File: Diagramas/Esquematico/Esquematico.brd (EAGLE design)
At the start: 64 x 80 mm, 48 parts, among them IC3 DS3231N_DIP, IC4 3071_SMD, J1 Modulo Pir, J2 RASPBERRYPI-40-PIN-GPIO_SMT, K1 SRD-05VDC-SL-C, K2 SRD-05VDC-SL-C, K3 SRD-05VDC-SL-C, K4 SRD-05VDC-SL-C, U1 RFM69HW-868S2

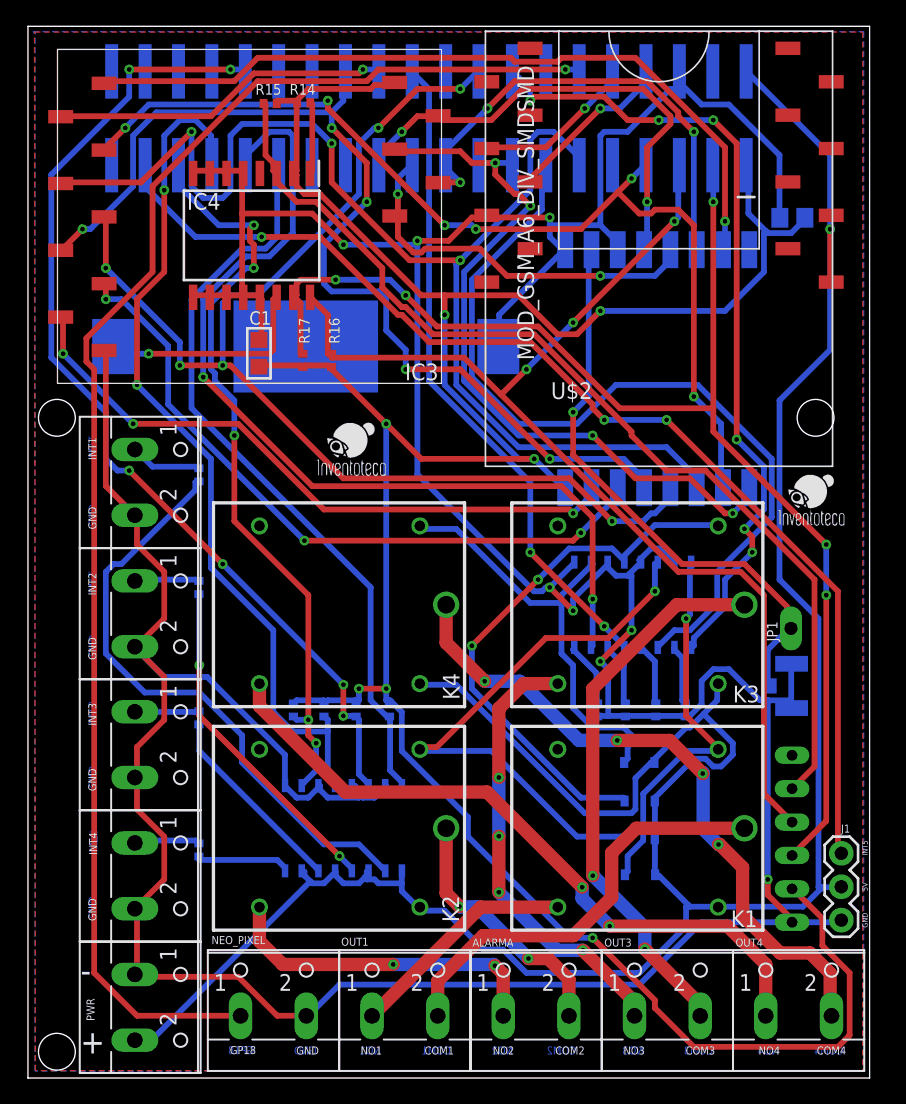
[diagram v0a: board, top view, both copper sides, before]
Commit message: Modulo Lora Eliminado
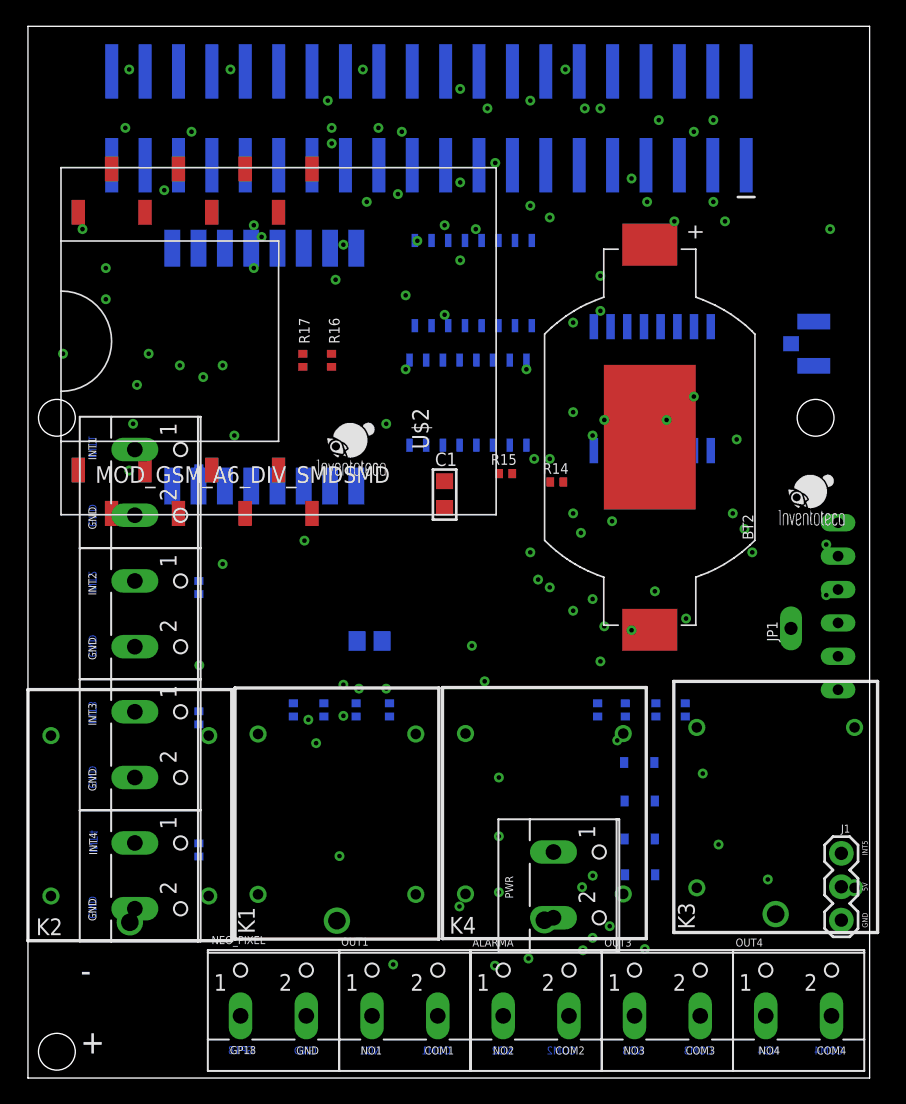
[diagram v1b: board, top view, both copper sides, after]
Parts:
- removed IC4: 3071_SMD, 3071:3071_SMD
- moved C3 45.5 mm to (26.0, 33.2)
- moved R14 34.7 mm to (40.2, 45.3)
- moved OK1 33.7 mm to (33.5, 51.4)
- moved R15 33.4 mm to (36.3, 46.0)
- moved PWR 33.2 mm to (41.2, 14.7)
- moved IC3 32.6 mm to (47.5, 52.4), flipped to the bottom
- moved K1 31.8 mm to (23.5, 12.0), turned to 90 degrees
- moved U1 29.9 mm to (18.0, 54.1), turned to 270 degrees
- moved U$2 29.8 mm to (19.1, 56.0), turned to 180 degrees
- moved OK2 27.3 mm to (33.9, 60.5)
- moved BT2 27.1 mm to (47.3, 48.7), flipped to the top, turned to 270 degrees
- moved ANT1 26.1 mm to (59.8, 55.9)
- moved K4 25.1 mm to (39.3, 12.0), turned to 90 degrees
- moved K2 25.1 mm to (7.75, 11.8), turned to 90 degrees
- moved K3 23.7 mm to (56.9, 12.5), turned to 90 degrees
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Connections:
- net 3.3V: no longer IC4.14
- net CS: no longer IC4.1
- net EN: no longer IC4.2
- net G0: no longer IC4.3
- net G1: no longer IC4.4
- net G2: no longer IC4.5
- net G3: no longer IC4.6
- net G4: no longer IC4.7
- net G5: no longer IC4.8
- net GND: no longer IC4.9
- net MISO: no longer IC4.10
- net MOSI: no longer IC4.11
- net RST_LORA: no longer IC4.12
- net SCK: no longer IC4.13
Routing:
- net GND: track 339.7 -> 0.00 mm
- net 3.3V: track 206.8 -> 0.00 mm
- net 5V: track 195.8 -> 0.00 mm
- net G18: track 110.8 -> 0.00 mm
- net SDA: track 98.9 -> 0.00 mm
- net G1: track 95.7 -> 0.00 mm
- net G2: track 91.3 -> 0.00 mm
- net INT5: track 87.4 -> 0.00 mm
- net SCL: track 87.0 -> 0.00 mm
- net G3: track 79.6 -> 0.00 mm
- net SQW: track 77.5 -> 0.00 mm
- net G0: track 77.2 -> 0.00 mm
- net INT2: track 76.8 -> 0.00 mm
- net OUT4: track 71.4 -> 0.00 mm
- net INT3: track 66.2 -> 0.00 mm
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- removed copper zone on layer 1, net GND
- removed copper zone on layer 16, net GND

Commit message: Sustitucion de la Bateria
Cambio de la bateria CR2032 por CR1220
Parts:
- removed BT2: BU2032SM-BT-GTR, BU2032SM-BT-GTR:BAT_BU2032SM-BT-GTR
- added B1: (no value), microbuilder:CR1220
- moved K3 2.09 mm to (54.9, 11.9)
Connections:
- net GND: now also B1.-; no longer BT2.2
- net VBAT: now also B1.+$1; no longer BT2.1
